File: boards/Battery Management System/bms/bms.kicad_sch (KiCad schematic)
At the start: 31 parts, among them J1 Screw_Terminal_01x05, J2 1986660-2, J3 1986660-2, Q1 PMOS, Q2 PMOS, Q3 PMOS, Q4 PMOS, Q5 NMOS, Q6 NMOS, Q7 NMOS, Q8 NMOS, U1 BD48L32G, U2 BD48L32G, U3 BD48L32G, U4 BD48L32G

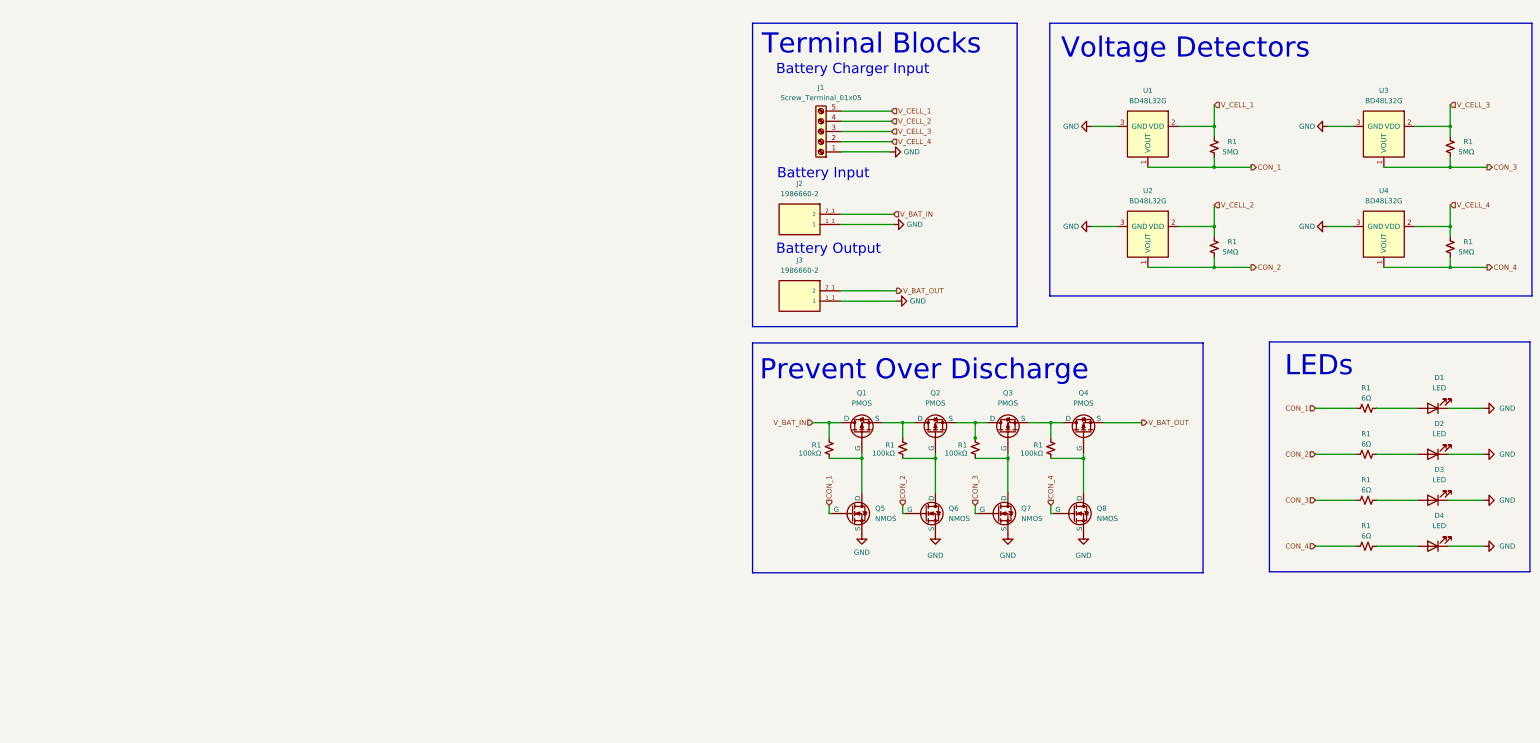
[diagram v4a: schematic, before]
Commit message: Changed mosfet circuit to relays on schematic
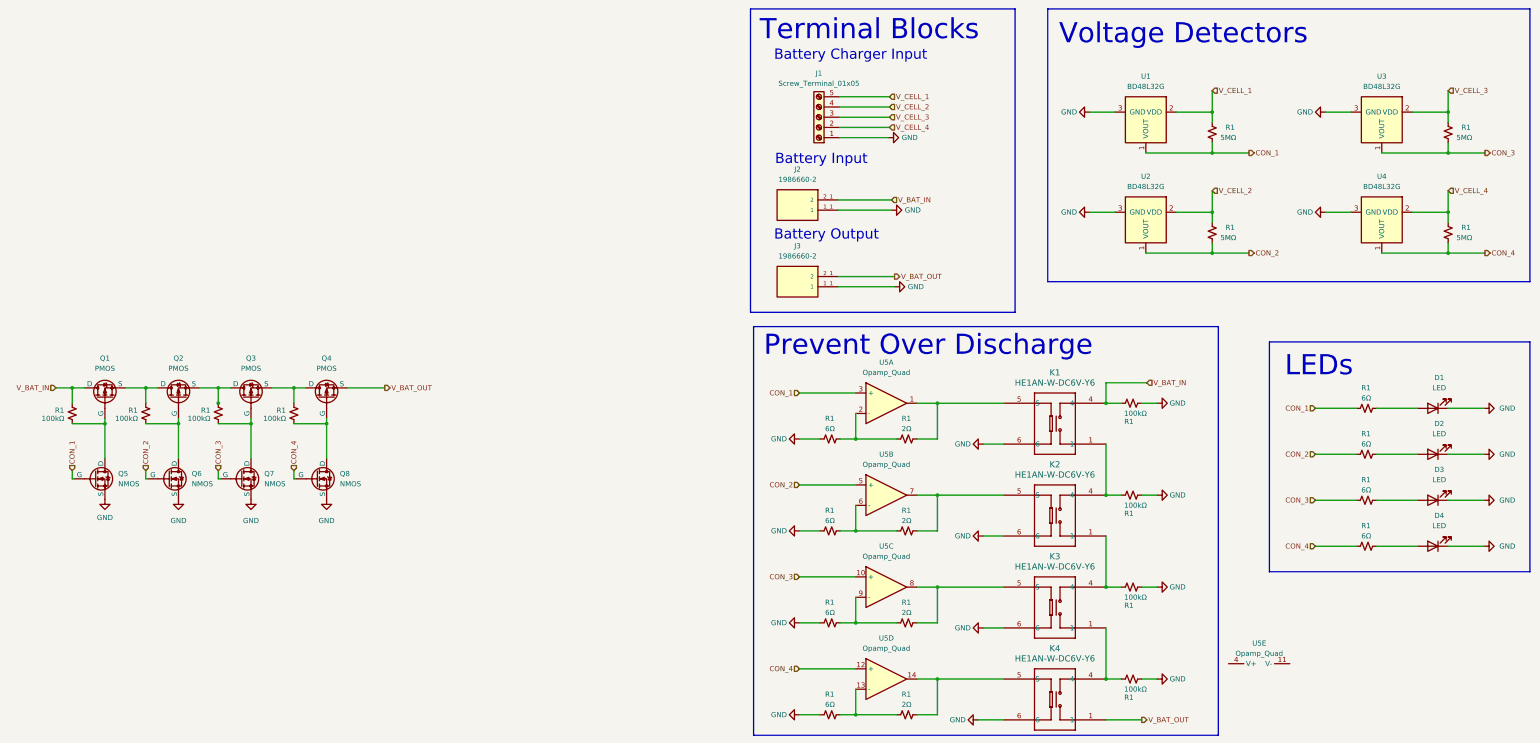
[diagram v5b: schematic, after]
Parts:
- added K1, K2, K3, K4: HE1AN-W-DC6V-Y6, HE1AN-W-DC6V_PAN, symbol 2024-03-08_00-12-08:HE1AN-W-DC6V-Y6
- added R1 (x4): 6Ω, Resistor_SMD:R_0805_2012Metric, symbol Device:R_Small_US
- added R1 (x4): 100kΩ, Resistor_SMD:R_0805_2012Metric, symbol Device:R_Small_US
- added R1 (x4): 2Ω, Resistor_SMD:R_0805_2012Metric, symbol Device:R_Small_US
- added U5: Opamp_Quad, symbol Device:Opamp_Quad
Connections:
- net CON_1: now also U5.3 (+)
- net CON_2: now also U5.5 (+)
- net CON_3: now also U5.10 (+)
- net CON_4: now also U5.12 (+)
- net GND: now also K1.6, K2.6, K3.6, K4.6, R1.1, R1.1, R1.1, R1.1, R1.1, R1.1, R1.1, R1.1
- net V_BAT_IN: now also K1.4, R1.2
- net V_BAT_OUT: now also K4.1
- new net: R1.1, R1.2, U5.13 (-)
- new net: K4.5, R1.2, U5.14
- new net: K3.1, K4.4, R1.2
- new net: R1.1, R1.2, U5.9 (-)
- new net: K3.5, R1.2, U5.8
- new net: K2.1, K3.4, R1.2
- new net: K1.1, K2.4, R1.2
- new net: K2.5, R1.2, U5.7
- new net: R1.1, R1.2, U5.6 (-)
- new net: K1.5, R1.2, U5.1
- new net: R1.1, R1.2, U5.2 (-)
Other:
- moved on the sheet: J1, J2, J3, Q1, Q2, Q3, Q4, Q5, Q6, Q7, Q8, R1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

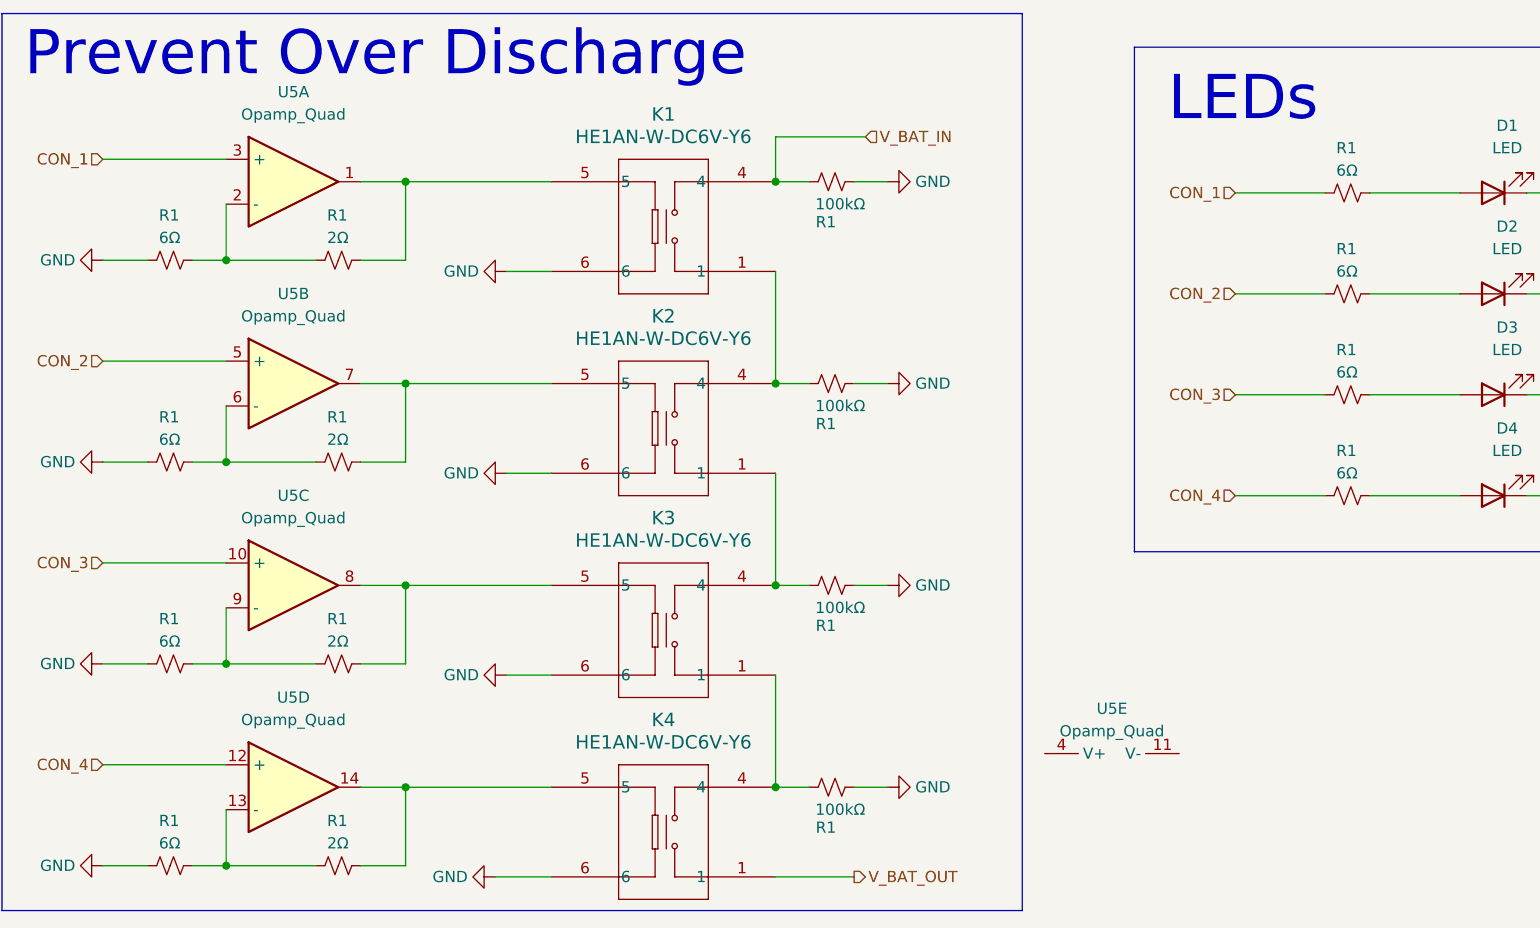
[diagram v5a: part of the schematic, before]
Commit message: Change resistor values
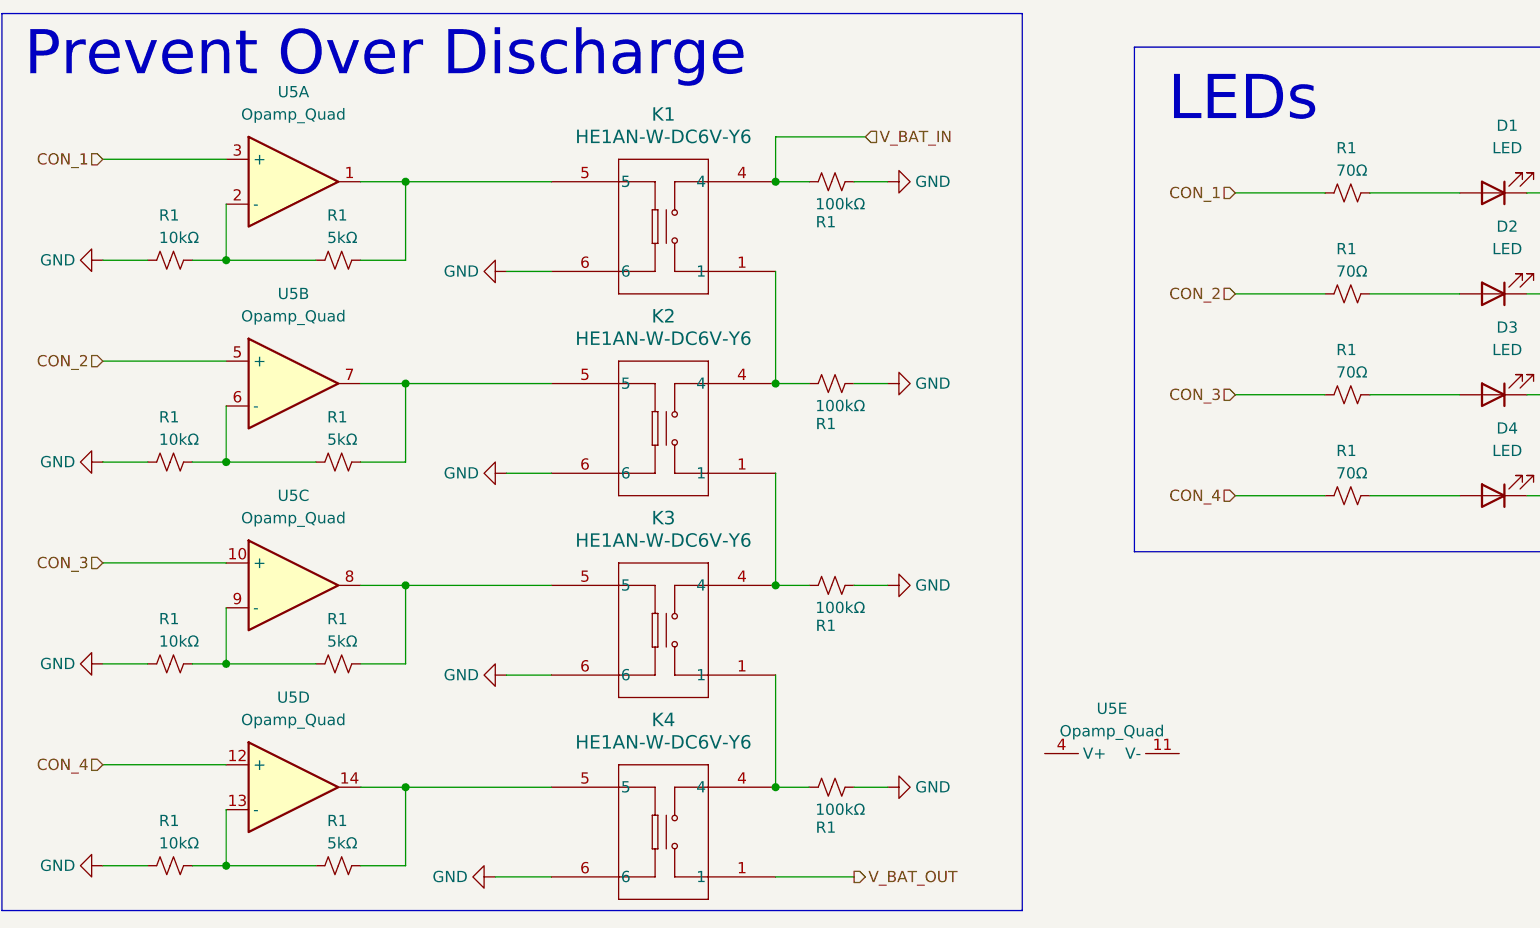
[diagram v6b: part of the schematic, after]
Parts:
- R1: value 6Ω -> 10kΩ
- R1: value 2Ω -> 5kΩ
- R1: value 6Ω -> 70Ω
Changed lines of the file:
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@@
       (effects (font (size 1.27 1.27)) (justify right))
     )
-    (property "Value" "6Ω" (at 39.37 187.96 90)
+    (property "Value" "10kΩ" (at 39.37 187.96 90)
       (effects (font (size 1.27 1.27)) (justify right))
     )
@@
       (effects (font (size 1.27 1.27)) (justify right))
     )
-    (property "Value" "2Ω" (at 58.42 165.1 90)
+    (property "Value" "5kΩ" (at 58.42 165.1 90)
       (effects (font (size 1.27 1.27)) (justify right))
     )
@@
       (effects (font (size 1.27 1.27)) (justify right))
     )
-    (property "Value" "6Ω" (at 39.37 142.24 90)
+    (property "Value" "10kΩ" (at 39.37 142.24 90)
       (effects (font (size 1.27 1.27)) (justify right))
     )
@@
       (effects (font (size 1.27 1.27)) (justify right))
     )
-    (property "Value" "2Ω" (at 58.42 187.96 90)
+    (property "Value" "5kΩ" (at 58.42 187.96 90)
       (effects (font (size 1.27 1.27)) (justify right))
     )
@@
       (effects (font (size 1.27 1.27)) (justify right))
     )
-    (property "Value" "6Ω" (at 172.72 111.76 90)
+    (property "Value" "70Ω" (at 172.72 111.76 90)
       (effects (font (size 1.27 1.27)) (justify right))
     )
@@
       (effects (font (size 1.27 1.27)) (justify right))
     )
-    (property "Value" "6Ω" (at 172.72 134.62 90)
+    (property "Value" "70Ω" (at 172.72 134.62 90)
       (effects (font (size 1.27 1.27)) (justify right))
     )
@@
       (effects (font (size 1.27 1.27)) (justify right))
     )
-    (property "Value" "6Ω" (at 172.72 146.05 90)
+    (property "Value" "70Ω" (at 172.72 146.05 90)
       (effects (font (size 1.27 1.27)) (justify right))
     )
@@
       (effects (font (size 1.27 1.27)) (justify right))
     )
-    (property "Value" "2Ω" (at 58.42 119.38 90)
+    (property "Value" "5kΩ" (at 58.42 119.38 90)
       (effects (font (size 1.27 1.27)) (justify right))
     )
@@
       (effects (font (size 1.27 1.27)) (justify right))
     )
-    (property "Value" "2Ω" (at 58.42 142.24 90)
+    (property "Value" "5kΩ" (at 58.42 142.24 90)
       (effects (font (size 1.27 1.27)) (justify right))
     )
@@
       (effects (font (size 1.27 1.27)) (justify right))
     )
-    (property "Value" "6Ω" (at 172.72 123.19 90)
+    (property "Value" "70Ω" (at 172.72 123.19 90)
       (effects (font (size 1.27 1.27)) (justify right))
     )
@@
       (effects (font (size 1.27 1.27)) (justify right))
     )
-    (property "Value" "6Ω" (at 39.37 165.1 90)
+    (property "Value" "10kΩ" (at 39.37 165.1 90)
       (effects (font (size 1.27 1.27)) (justify right))
     )
@@
       (effects (font (size 1.27 1.27)) (justify right))
     )
-    (property "Value" "6Ω" (at 39.37 119.38 90)
-      (effects (font (size 1.27 1.27)) (justify right))
-    )
+    (property "Value" "10kΩ" (at 39.37 119.38 90)
+      (effects (font (size 1.27 1.27)) (justify right))
+    )

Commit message: Worked on schematic and PCB
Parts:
- removed K2, K3, K4: HE1AN-W-DC6V-Y6, HE1AN-W-DC6V_PAN, symbol 2024-03-08_00-12-08:HE1AN-W-DC6V-Y6
- removed Q1, Q2, Q3, Q4: PMOS, BSS84_7_F:SOT-23_DIO, symbol Simulation_SPICE:PMOS
- removed Q5, Q6, Q7, Q8: NMOS, BSS138:SOT95P240X111-3N, symbol Simulation_SPICE:NMOS
- removed R1 (x3): 10kΩ, Resistor_SMD:R_0805_2012Metric, symbol Device:R_Small_US
- removed R1 (x7): 100kΩ, Resistor_SMD:R_0805_2012Metric, symbol Device:R_Small_US
- removed R1 (x3): 5kΩ, Resistor_SMD:R_0805_2012Metric, symbol Device:R_Small_US
- removed unit 4 of U5
- removed unit 3 of U5
- removed unit 5 of U5
- removed unit 2 of U5
- added U6, U7: 74AUC2G08, footprints:D14-L, symbol 74xGxx:74AUC2G08
- K1: footprint HE1AN-W-DC6V_PAN -> footprints:HE1AN-W-DC6V_PAN
- U5: footprint (none) -> footprints:SOT23_DBV_5_TEX-L
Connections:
- net CON_1: now also U6.1; no longer U5.3 (+)
- net CON_2: now also U6.2
- net CON_3: now also U6.6
- net CON_4: now also U7.6
- net V_BAT_OUT: now also K1.1
- new net: U6.5, U6.7
- new net: U6.3, U7.5
- new net: U5.3 (+), U7.3
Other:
- moved on the sheet: K1, R1, U5A

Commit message: Edited schematic and PCB
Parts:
- renumbered U7 to U6
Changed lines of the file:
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@@
   (symbol (lib_id "74xGxx:74AUC2G08") (at 114.3 152.4 0) (unit 2)
     (in_bom yes) (on_board yes) (dnp no) (fields_autoplaced)
-    (property "Reference" "U7" (at 113.0189 142.24 0)
+    (property "Reference" "U6" (at 113.0189 142.24 0)
       (effects (font (size 1.27 1.27)))
     )
@@
       (project "bms"
         (path "/e0ec80f6-0ac5-448e-a052-7eb38c8b1976"
-          (reference "U7") (unit 2)
+          (reference "U6") (unit 2)
         )
       )
